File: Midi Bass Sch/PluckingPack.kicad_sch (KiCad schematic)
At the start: 24 parts, among them Q1 BDW93C, Q2 BDW93C, Q3 BDW93C, Q4 BDW93C, Q5 BDW93C, Q6 BDW93C, Q7 BDW93C, Q8 BDW93C

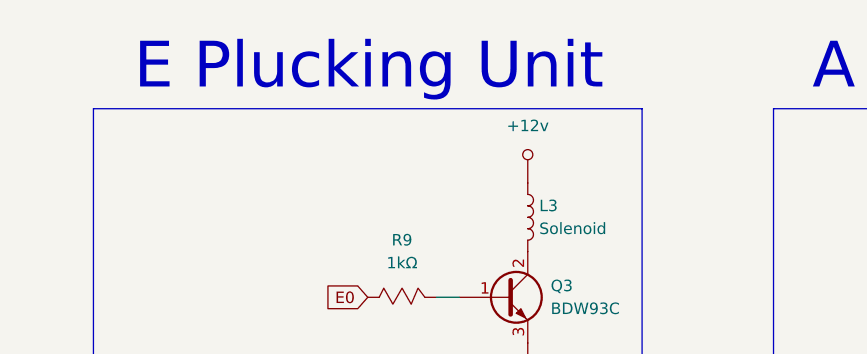
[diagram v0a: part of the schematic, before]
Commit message: updated e slave added solenoid for slave added reset button
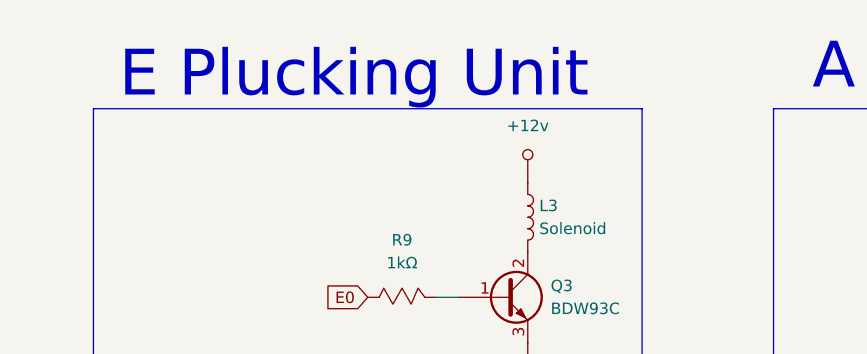
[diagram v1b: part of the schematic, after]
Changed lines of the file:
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@@
 	(text "E Plucking Unit"
 		(exclude_from_sim no)
-		(at 162.687 20.193 0)
+		(at 161.036 21.082 0)
 		(effects
 			(font

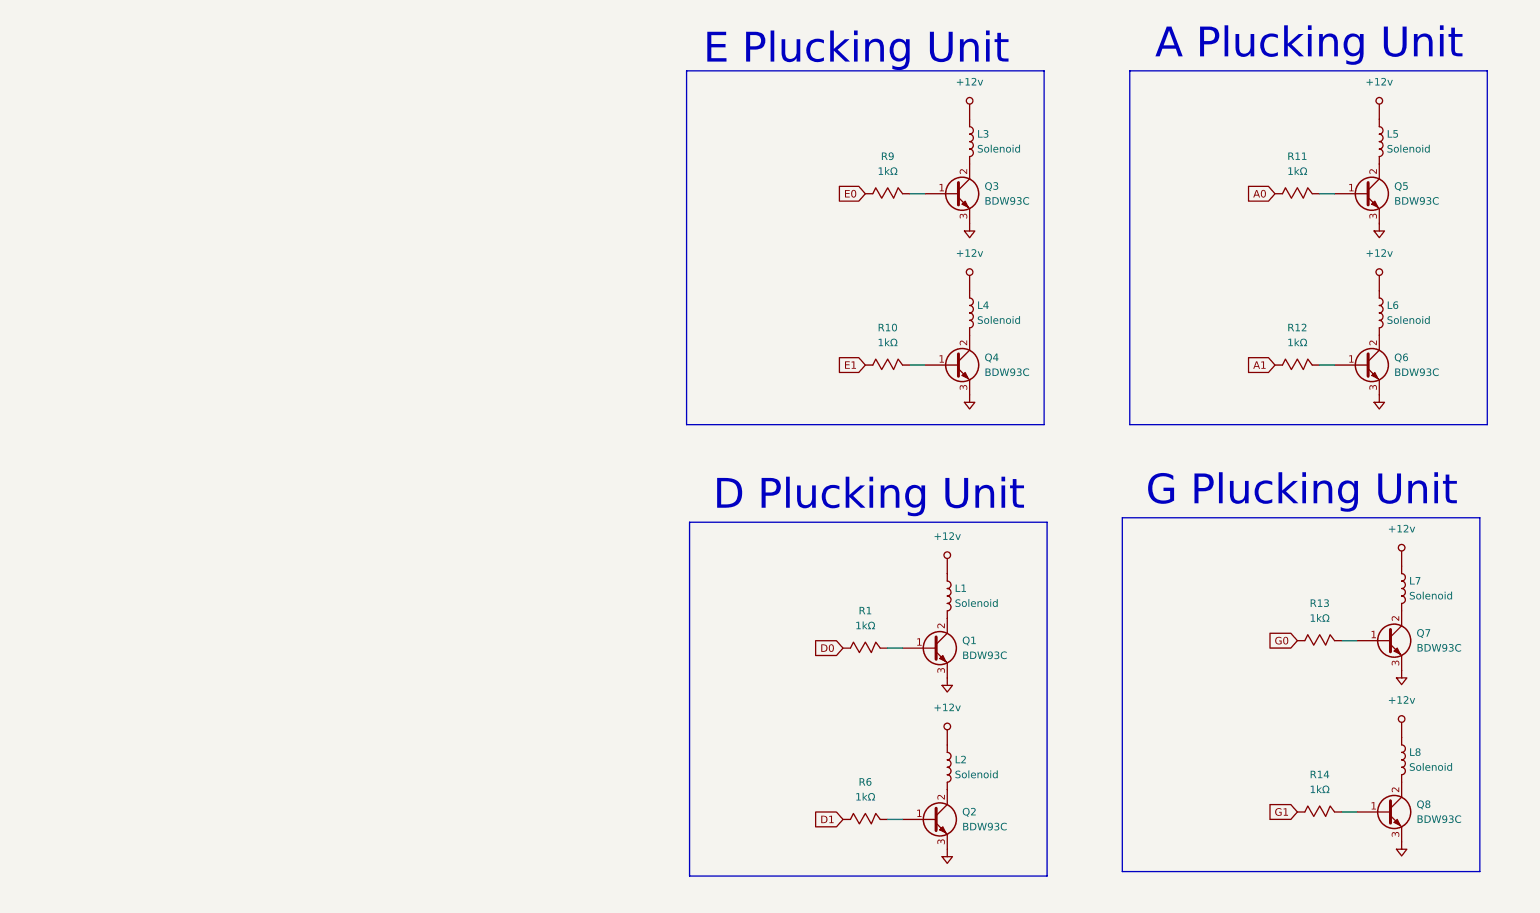
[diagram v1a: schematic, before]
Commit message: added opto isolation to plucking solenoids
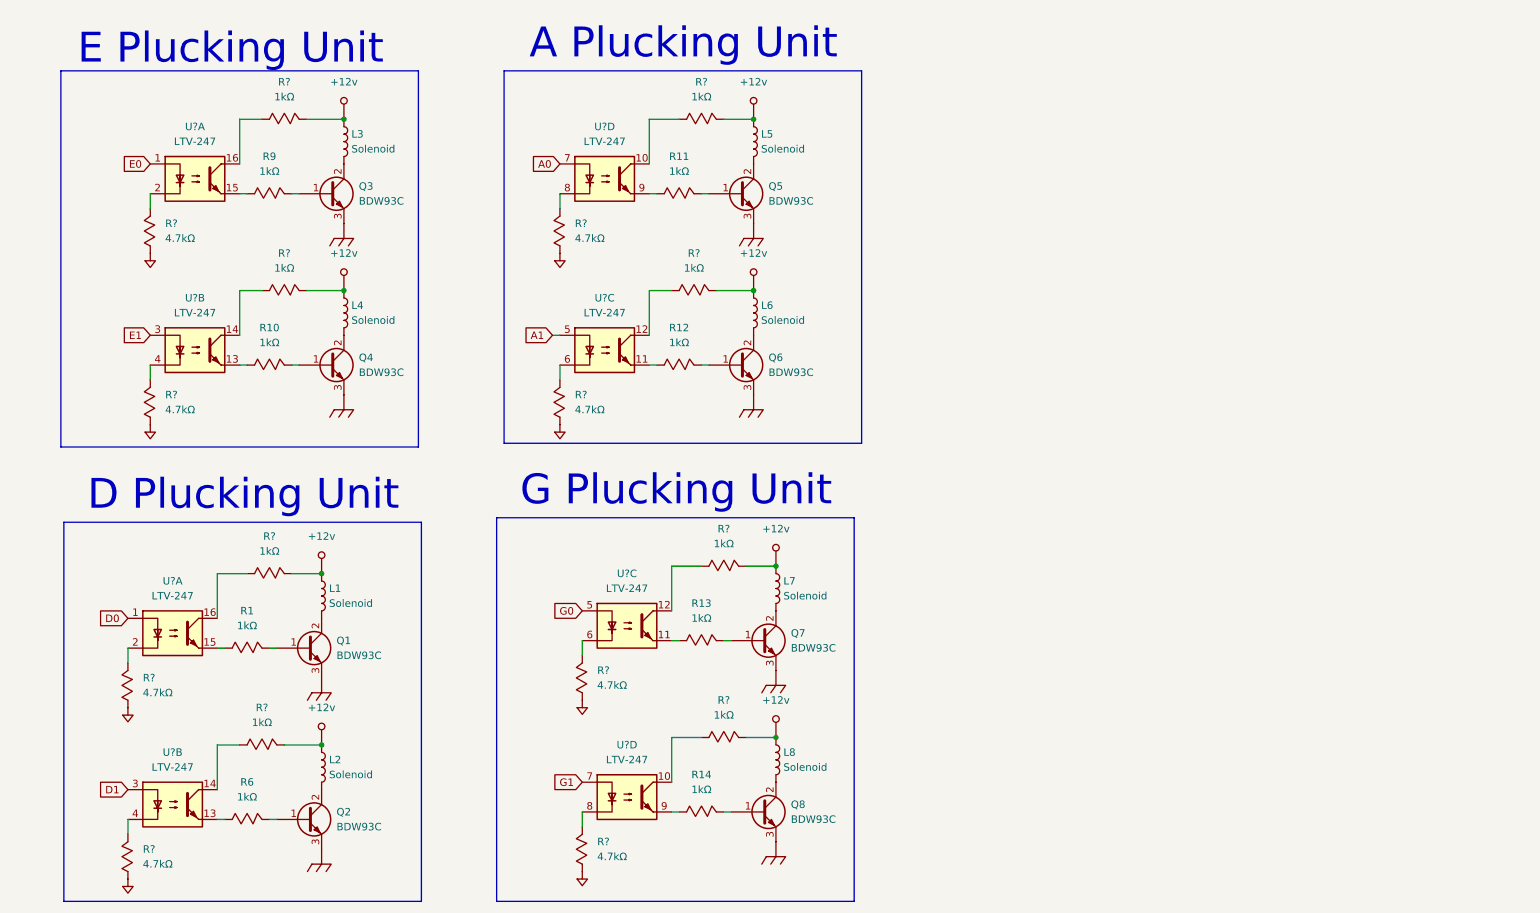
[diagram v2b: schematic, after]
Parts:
- added R? (x8): 1kΩ, symbol Custom Symbols:Resistor_Mod
- added R? (x8): 4.7kΩ, symbol Custom Symbols:Resistor_Mod
- added U? (x8): LTV-247, Package_SO:SOP-16_4.4x10.4mm_P1.27mm, symbol Isolator:LTV-247
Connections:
- net +12v: now also R?.2, R?.2, R?.2, R?.2, R?.2, R?.2, R?.2, R?.2
- net A0: now also U?.7; no longer R11.1
- net A1: now also U?.5; no longer R12.1
- net D0: now also U?.1; no longer R1.1
- net D1: now also U?.3; no longer R6.1
- net E0: now also U?.1; no longer R9.1
- net E1: now also U?.3; no longer R10.1
- net G0: now also U?.5; no longer R13.1
- net G1: now also U?.7; no longer R14.1
- net GND: now also R?.1, R?.1, R?.1, R?.1, R?.1, R?.1, R?.1, R?.1; no longer Q1.3 (E), Q2.3 (E), Q3.3 (E), Q4.3 (E), Q5.3 (E), Q6.3 (E), Q7.3 (E), Q8.3 (E)
- new net: R12.1, U?.11
- new net: R?.1, U?.12 (x2)
- new net: R?.2, U?.6 (x2)
- new net: R6.1, U?.13
- new net: R?.1, U?.14 (x2)
- new net: R?.2, U?.4 (x2)
- new net: R1.1, U?.15
- new net: R?.1, U?.10 (x2)
- new net: R?.2, U?.8 (x2)
- new net: R?.2, U?.2 (x2)
- new net: R9.1, U?.15
- new net: R10.1, U?.13
- new net: R13.1, U?.11
- new net: R14.1, U?.9
- new net: R?.1, U?.16 (x2)
- new net: R11.1, U?.9
- new net Chassis_GND: Q1.3 (E), Q2.3 (E), Q3.3 (E), Q4.3 (E), Q5.3 (E), Q6.3 (E), Q7.3 (E), Q8.3 (E)
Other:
- moved on the sheet: L1, L2, L3, L4, L5, L6, L7, L8, Q1, Q2, Q3, Q4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

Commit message: working on system overview of report
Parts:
- gave numbers to parts that had none: 18
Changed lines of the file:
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@@
 		(dnp no)
 		(fields_autoplaced yes)
-		(property "Reference" "U?"
+		(property "Reference" "U12"
 			(at 118.11 63.5 0)
 			(effects
@@
 			(project ""
 				(path "/06818073-fb22-48ee-acc5-6dedd827034e/673444b1-2638-4f61-b545-e7cdf999c0e0/a9c725c7-a2b4-4653-bf22-cca353cf3c61"
-					(reference "U?")
+					(reference "U12")
 					(unit 3)
 				)
@@
 		(dnp no)
 		(fields_autoplaced yes)
-		(property "Reference" "R?"
+		(property "Reference" "R103"
 			(at 133.35 55.88 0)
 			(effects
@@
 			(project "Midi Bass Sch"
 				(path "/06818073-fb22-48ee-acc5-6dedd827034e/673444b1-2638-4f61-b545-e7cdf999c0e0/a9c725c7-a2b4-4653-bf22-cca353cf3c61"
-					(reference "R?")
+					(reference "R103")
 					(unit 1)
 				)
@@
 		(dnp no)
 		(fields_autoplaced yes)
-		(property "Reference" "U?"
+		(property "Reference" "U12"
 			(at 44.45 140.97 0)
 			(effects
@@
 			(project ""
 				(path "/06818073-fb22-48ee-acc5-6dedd827034e/673444b1-2638-4f61-b545-e7cdf999c0e0/a9c725c7-a2b4-4653-bf22-cca353cf3c61"
-					(reference "U?")
+					(reference "U12")
 					(unit 2)
 				)
@@
 		(dnp no)
 		(fields_autoplaced yes)
-		(property "Reference" "R?"
+		(property "Reference" "R101"
 			(at 116.84 126.9999 90)
 			(effects
@@
 			(project "Midi Bass Sch"
 				(path "/06818073-fb22-48ee-acc5-6dedd827034e/673444b1-2638-4f61-b545-e7cdf999c0e0/a9c725c7-a2b4-4653-bf22-cca353cf3c61"
-					(reference "R?")
+					(reference "R101")
 					(unit 1)
 				)
@@
 		(dnp no)
 		(fields_autoplaced yes)
-		(property "Reference" "R?"
+		(property "Reference" "R104"
 			(at 134.62 26.67 0)
 			(effects
@@
 			(project "Midi Bass Sch"
 				(path "/06818073-fb22-48ee-acc5-6dedd827034e/673444b1-2638-4f61-b545-e7cdf999c0e0/a9c725c7-a2b4-4653-bf22-cca353cf3c61"
-					(reference "R?")
+					(reference "R104")
 					(unit 1)
 				)
@@
 		(dnp no)
 		(fields_autoplaced yes)
-		(property "Reference" "R?"
+		(property "Reference" "R99"
 			(at 113.03 50.7999 90)
 			(effects
@@
 			(project "Midi Bass Sch"
 				(path "/06818073-fb22-48ee-acc5-6dedd827034e/673444b1-2638-4f61-b545-e7cdf999c0e0/a9c725c7-a2b4-4653-bf22-cca353cf3c61"
-					(reference "R?")
+					(reference "R99")
 					(unit 1)
 				)
@@
 		(dnp no)
 		(fields_autoplaced yes)
-		(property "Reference" "R?"
+		(property "Reference" "R102"
 			(at 116.84 156.2099 90)
 			(effects
@@
 			(project "Midi Bass Sch"
 				(path "/06818073-fb22-48ee-acc5-6dedd827034e/673444b1-2638-4f61-b545-e7cdf999c0e0/a9c725c7-a2b4-4653-bf22-cca353cf3c61"
-					(reference "R?")
+					(reference "R102")
 					(unit 1)
 				)
@@
 		(dnp no)
 		(fields_autoplaced yes)
-		(property "Reference" "R?"
+		(property "Reference" "R91"
 			(at 39.37 128.2699 90)
 			(effects
@@
 			(project "Midi Bass Sch"
 				(path "/06818073-fb22-48ee-acc5-6dedd827034e/673444b1-2638-4f61-b545-e7cdf999c0e0/a9c725c7-a2b4-4653-bf22-cca353cf3c61"
-					(reference "R?")
+					(reference "R91")
 					(unit 1)
 				)
@@
 		(dnp no)
 		(fields_autoplaced yes)
-		(property "Reference" "R?"
+		(property "Reference" "R106"
 			(at 138.43 132.08 0)
 			(effects
@@
 			(project "Midi Bass Sch"
 				(path "/06818073-fb22-48ee-acc5-6dedd827034e/673444b1-2638-4f61-b545-e7cdf999c0e0/a9c725c7-a2b4-4653-bf22-cca353cf3c61"
-					(reference "R?")
+					(reference "R106")
 					(unit 1)
 				)
@@
 		(dnp no)
 		(fields_autoplaced yes)
-		(property "Reference" "R?"
+		(property "Reference" "R105"
 			(at 138.43 102.87 0)
 			(effects
@@
 			(project "Midi Bass Sch"
 				(path "/06818073-fb22-48ee-acc5-6dedd827034e/673444b1-2638-4f61-b545-e7cdf999c0e0/a9c725c7-a2b4-4653-bf22-cca353cf3c61"
-					(reference "R?")
+					(reference "R105")
 					(unit 1)
 				)
@@
 		(dnp no)
 		(fields_autoplaced yes)
-		(property "Reference" "U?"
+		(property "Reference" "U13"
 			(at 121.92 110.49 0)
 			(effects
@@
 			(project ""
 				(path "/06818073-fb22-48ee-acc5-6dedd827034e/673444b1-2638-4f61-b545-e7cdf999c0e0/a9c725c7-a2b4-4653-bf22-cca353cf3c61"
-					(reference "U?")
+					(reference "U13")
 					(unit 3)
 				)
@@
 		(dnp no)
 		(fields_autoplaced yes)
-		(property "Reference" "R?"
+		(property "Reference" "R96"
 			(at 60.96 104.14 0)
 			(effects
@@
 			(project "Midi Bass Sch"
 				(path "/06818073-fb22-48ee-acc5-6dedd827034e/673444b1-2638-4f61-b545-e7cdf999c0e0/a9c725c7-a2b4-4653-bf22-cca353cf3c61"
-					(reference "R?")
+					(reference "R96")
 					(unit 1)
 				)
@@
 		(dnp no)
 		(fields_autoplaced yes)
-		(property "Reference" "R?"
+		(property "Reference" "R95"
 			(at 59.69 133.35 0)
 			(effects
@@
 			(project "Midi Bass Sch"
 				(path "/06818073-fb22-48ee-acc5-6dedd827034e/673444b1-2638-4f61-b545-e7cdf999c0e0/a9c725c7-a2b4-4653-bf22-cca353cf3c61"
-					(reference "R?")
+					(reference "R95")
 					(unit 1)
 				)
@@
 		(dnp no)
 		(fields_autoplaced yes)
-		(property "Reference" "U?"
+		(property "Reference" "U12"
 			(at 118.11 34.29 0)
 			(effects
@@
 			(project ""
 				(path "/06818073-fb22-48ee-acc5-6dedd827034e/673444b1-2638-4f61-b545-e7cdf999c0e0/a9c725c7-a2b4-4653-bf22-cca353cf3c61"
-					(reference "U?")
+					(reference "U12")
 					(unit 4)
 				)
@@
 		(dnp no)
 		(fields_autoplaced yes)
-		(property "Reference" "R?"
+		(property "Reference" "R98"
 			(at 63.5 55.88 0)
 			(effects
@@
 			(project "Midi Bass Sch"
 				(path "/06818073-fb22-48ee-acc5-6dedd827034e/673444b1-2638-4f61-b545-e7cdf999c0e0/a9c725c7-a2b4-4653-bf22-cca353cf3c61"
-					(reference "R?")
+					(reference "R98")
 					(unit 1)
 				)
@@
 		(dnp no)
 		(fields_autoplaced yes)
-		(property "Reference" "R?"
+		(property "Reference" "R93"
 			(at 43.18 50.7999 90)
 			(effects
@@
 			(project "Midi Bass Sch"
 				(path "/06818073-fb22-48ee-acc5-6dedd827034e/673444b1-2638-4f61-b545-e7cdf999c0e0/a9c725c7-a2b4-4653-bf22-cca353cf3c61"
-					(reference "R?")
+					(reference "R93")
 					(unit 1)
 				)
@@
 		(dnp no)
 		(fields_autoplaced yes)
-		(property "Reference" "R?"
+		(property "Reference" "R94"
 			(at 43.18 80.0099 90)
 			(effects
@@
 			(project "Midi Bass Sch"
 				(path "/06818073-fb22-48ee-acc5-6dedd827034e/673444b1-2638-4f61-b545-e7cdf999c0e0/a9c725c7-a2b4-4653-bf22-cca353cf3c61"
-					(reference "R?")
+					(reference "R94")
 					(unit 1)
 				)
@@
 		(dnp no)
 		(fields_autoplaced yes)
-		(property "Reference" "R?"
+		(property "Reference" "R97"
 			(at 63.5 26.67 0)
 			(effects
@@
 			(project "Midi Bass Sch"
 				(path "/06818073-fb22-48ee-acc5-6dedd827034e/673444b1-2638-4f61-b545-e7cdf999c0e0/a9c725c7-a2b4-4653-bf22-cca353cf3c61"
-					(reference "R?")
+					(reference "R97")
 					(unit 1)
 				)
@@
 		(dnp no)
 		(fields_autoplaced yes)
-		(property "Reference" "R?"
+		(property "Reference" "R92"
 			(at 39.37 157.4799 90)
 			(effects
@@
 			(project "Midi Bass Sch"
 				(path "/06818073-fb22-48ee-acc5-6dedd827034e/673444b1-2638-4f61-b545-e7cdf999c0e0/a9c725c7-a2b4-4653-bf22-cca353cf3c61"
-					(reference "R?")
+					(reference "R92")
 					(unit 1)
 				)
@@
 		(dnp no)
 		(fields_autoplaced yes)
-		(property "Reference" "U?"
+		(property "Reference" "U13"
 			(at 48.26 63.5 0)
 			(effects
@@
 			(project ""
 				(path "/06818073-fb22-48ee-acc5-6dedd827034e/673444b1-2638-4f61-b545-e7cdf999c0e0/a9c725c7-a2b4-4653-bf22-cca353cf3c61"
-					(reference "U?")
+					(reference "U13")
 					(unit 2)
 				)
@@
 		(dnp no)
 		(fields_autoplaced yes)
-		(property "Reference" "R?"
+		(property "Reference" "R100"
 			(at 113.03 80.0099 90)
 			(effects
@@
 			(project "Midi Bass Sch"
 				(path "/06818073-fb22-48ee-acc5-6dedd827034e/673444b1-2638-4f61-b545-e7cdf999c0e0/a9c725c7-a2b4-4653-bf22-cca353cf3c61"
-					(reference "R?")
+					(reference "R100")
 					(unit 1)
 				)
@@
 		(dnp no)
 		(fields_autoplaced yes)
-		(property "Reference" "U?"
+		(property "Reference" "U13"
 			(at 121.92 139.7 0)
 			(effects
@@
 			(project ""
 				(path "/06818073-fb22-48ee-acc5-6dedd827034e/673444b1-2638-4f61-b545-e7cdf999c0e0/a9c725c7-a2b4-4653-bf22-cca353cf3c61"
-					(reference "U?")
+					(reference "U13")
 					(unit 4)
 				)
@@
 		(dnp no)
 		(fields_autoplaced yes)
-		(property "Reference" "U?"
+		(property "Reference" "U13"
 			(at 48.26 34.29 0)
 			(effects
@@
 			(project ""
 				(path "/06818073-fb22-48ee-acc5-6dedd827034e/673444b1-2638-4f61-b545-e7cdf999c0e0/a9c725c7-a2b4-4653-bf22-cca353cf3c61"
-					(reference "U?")
+					(reference "U13")
 					(unit 1)
 				)
@@
 		(dnp no)
 		(fields_autoplaced yes)
-		(property "Reference" "U?"
+		(property "Reference" "U12"
 			(at 44.45 111.76 0)
 			(effects
@@
 			(project ""
 				(path "/06818073-fb22-48ee-acc5-6dedd827034e/673444b1-2638-4f61-b545-e7cdf999c0e0/a9c725c7-a2b4-4653-bf22-cca353cf3c61"
-					(reference "U?")
+					(reference "U12")
 					(unit 1)
 				)
